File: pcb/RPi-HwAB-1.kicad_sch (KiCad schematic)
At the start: 5 parts, among them U1 CAT24C256

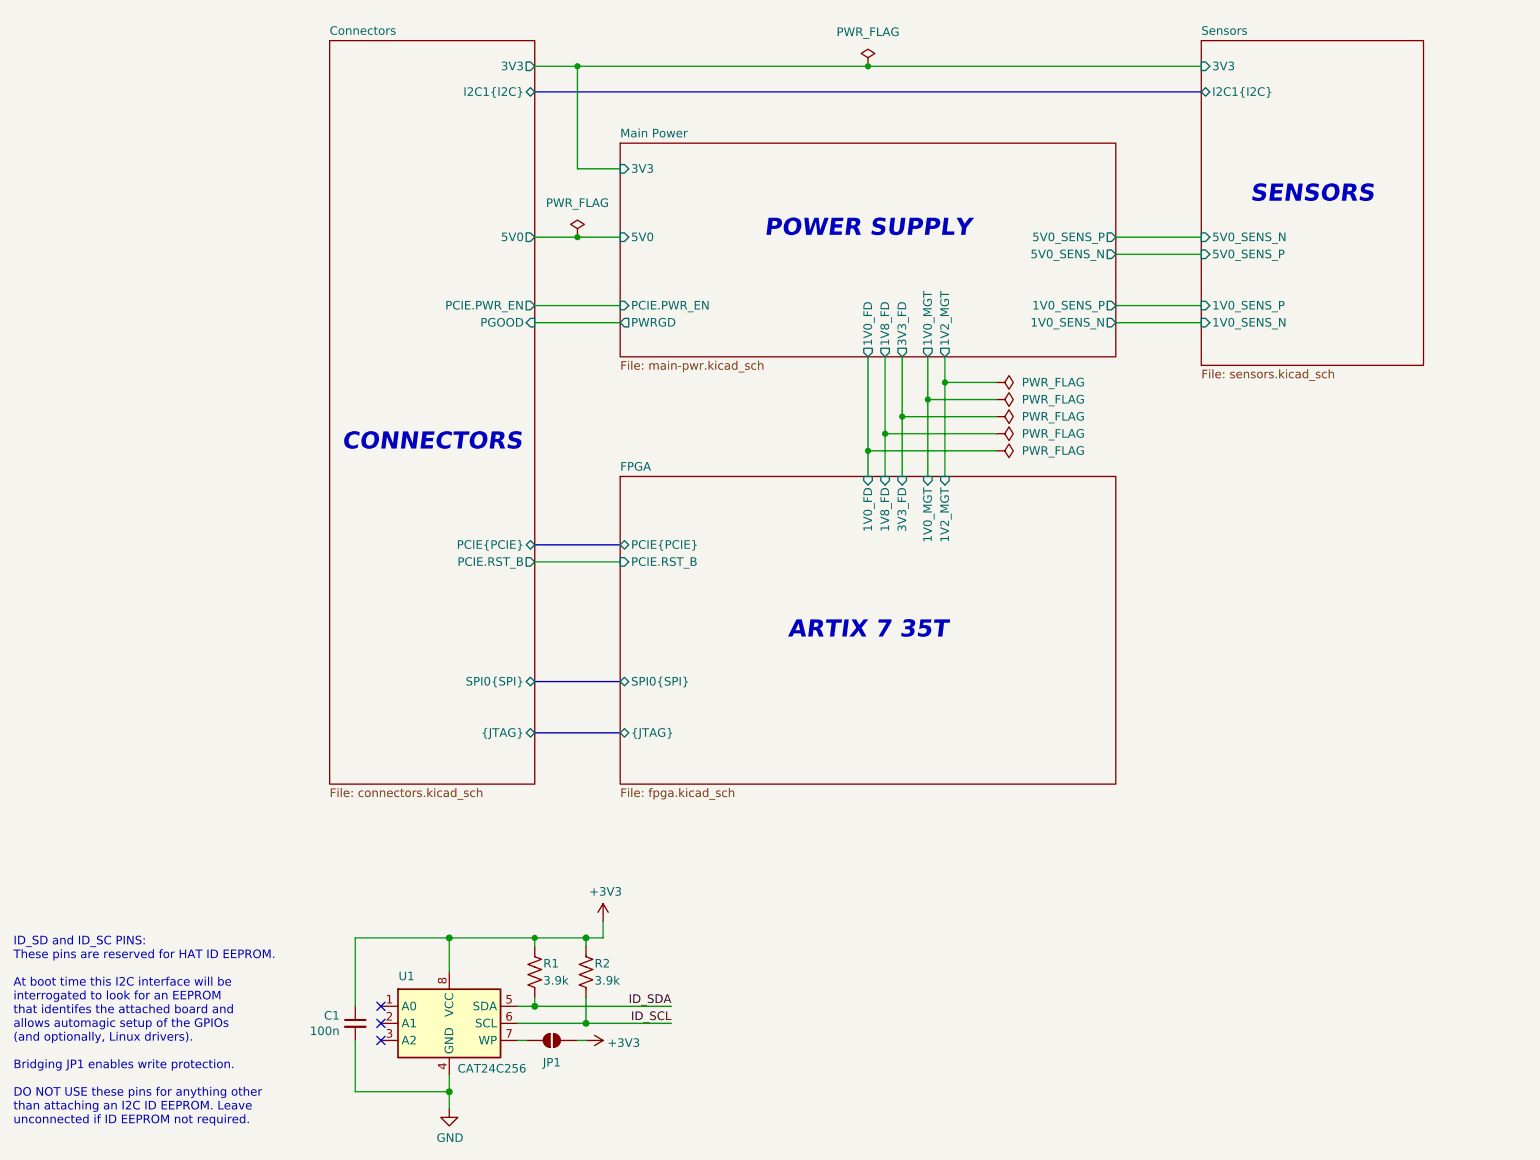
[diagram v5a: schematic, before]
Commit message: defined memory pinouts
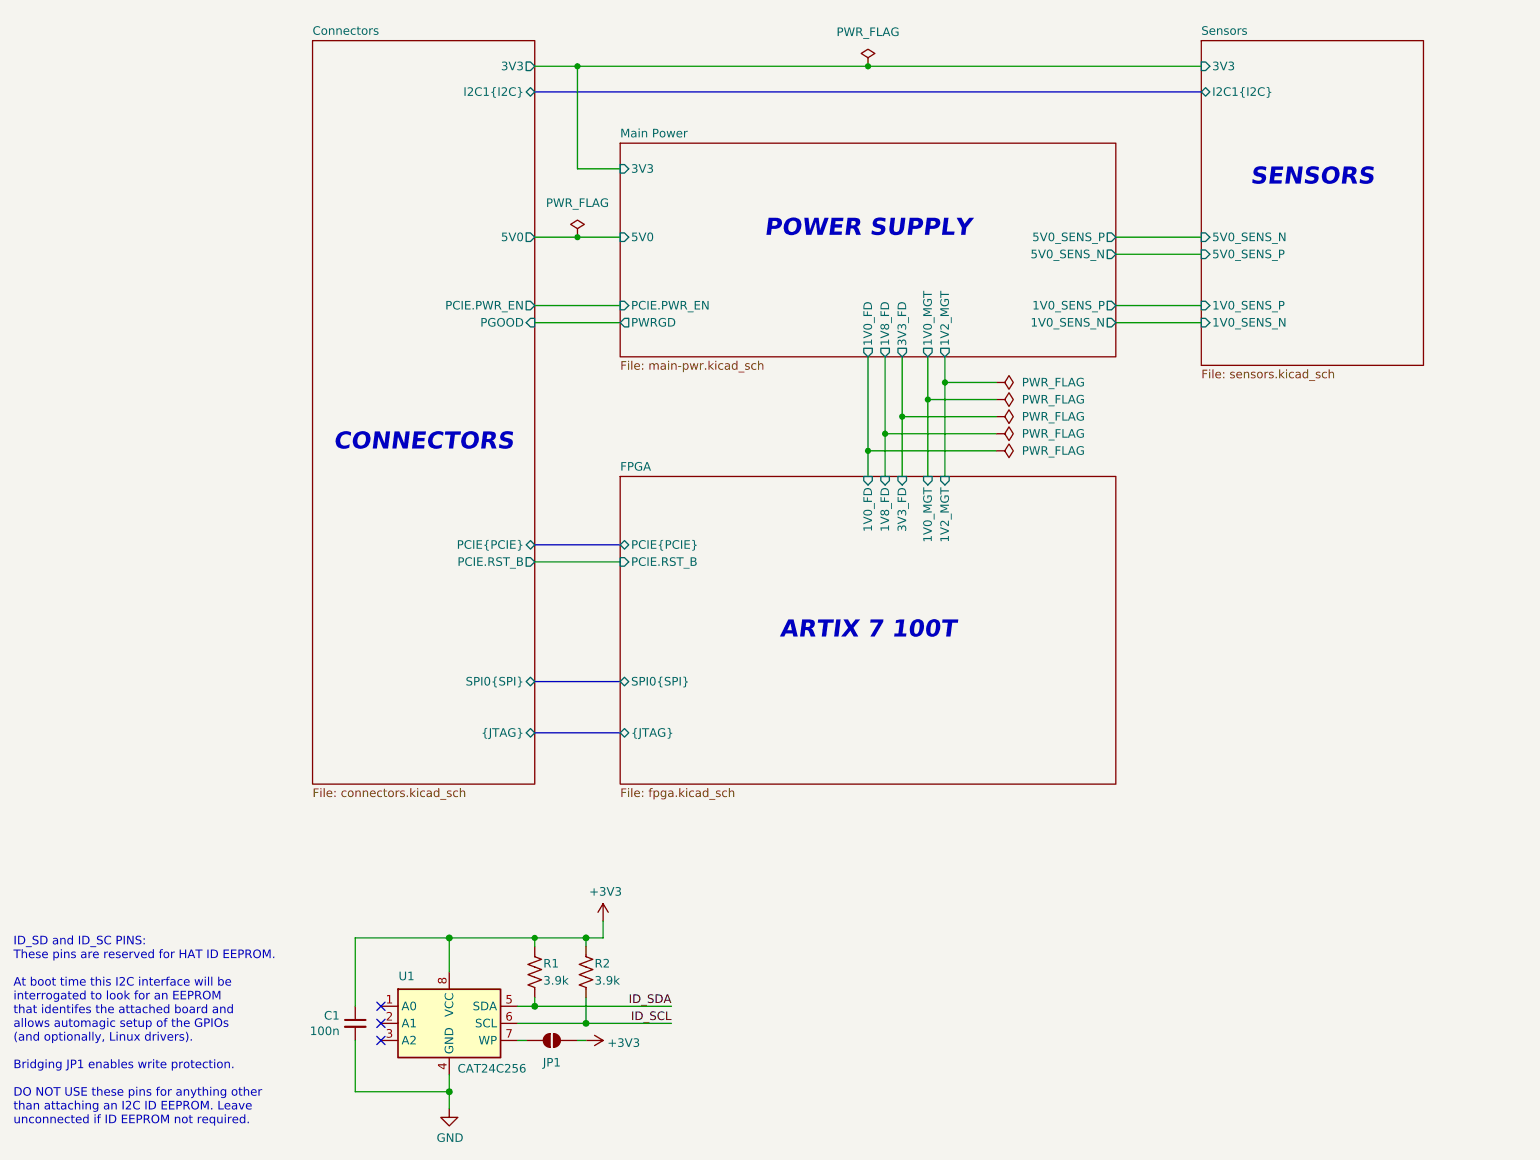
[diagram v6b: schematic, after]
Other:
- note added: "ARTIX 7 100T"
- note removed: "ARTIX 7 35T"
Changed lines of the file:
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@@
 		(members "MOSI" "MISO" "SCK" "CS0" "CS1")
 	)
-	(text "ARTIX 7 35T"
+	(text "ARTIX 7 100T"
 		(exclude_from_sim no)
 		(at 143.51 119.38 0)
@@
 	(text "SENSORS"
 		(exclude_from_sim no)
-		(at 209.55 54.61 0)
+		(at 209.55 52.07 0)
 		(effects
 			(font
@@
 	(text "CONNECTORS"
 		(exclude_from_sim no)
-		(at 78.74 91.44 0)
+		(at 77.47 91.44 0)
 		(effects
 			(font
@@
 		(at 143.51 35.56)
 		(diameter 0)
-		(color 0 0 0 0)
+		(color 0 0 255 1)
 	)
 	(junction
@@
 		(at 100.33 60.96)
 		(diameter 0)
-		(color 0 0 0 0)
+		(color 255 0 0 1)
 	)
 	(no_connect
@@
 		(on_board yes)
 		(dnp no)
-		(property "Reference" "#PWR07"
+		(property "Reference" "#PWR03"
 			(at 104.14 166.37 0)
 			(effects
@@
 			(project "RaspberryPi-HAT"
 				(path "/e63e39d7-6ac0-4ffd-8aa3-1841a4541b55"
-					(reference "#PWR07")
+					(reference "#PWR03")
 					(unit 1)
 				)
@@
 		(dnp no)
 		(fields_autoplaced yes)
-		(property "Reference" "#FLG07"
+		(property "Reference" "#FLG05"
 			(at 164.465 87.63 0)
 			(effects
@@
 			(project "RPi-HwAB-1"
 				(path "/e63e39d7-6ac0-4ffd-8aa3-1841a4541b55"
-					(reference "#FLG07")
+					(reference "#FLG05")
 					(unit 1)
 				)
@@
 		(dnp no)
 		(fields_autoplaced yes)
-		(property "Reference" "#FLG08"
+		(property "Reference" "#FLG04"
 			(at 164.465 85.09 0)
 			(effects
@@
 			(project "RPi-HwAB-1"
 				(path "/e63e39d7-6ac0-4ffd-8aa3-1841a4541b55"
-					(reference "#FLG08")
+					(reference "#FLG04")
 					(unit 1)
 				)
@@
 		(dnp no)
 		(fields_autoplaced yes)
-		(property "Reference" "#FLG011"
+		(property "Reference" "#FLG02"
 			(at 143.51 33.655 0)
 			(effects
@@
 			(project "RPi-HwAB-1"
 				(path "/e63e39d7-6ac0-4ffd-8aa3-1841a4541b55"
-					(reference "#FLG011")
+					(reference "#FLG02")
 					(unit 1)
 				)
@@
 		(on_board yes)
 		(dnp no)
-		(property "Reference" "#PWR05"
+		(property "Reference" "#PWR01"
 			(at 81.28 196.85 0)
 			(effects
@@
 			(project "RaspberryPi-HAT"
 				(path "/e63e39d7-6ac0-4ffd-8aa3-1841a4541b55"
-					(reference "#PWR05")
+					(reference "#PWR01")
 					(unit 1)
 				)
@@
 		(on_board yes)
 		(dnp no)
-		(property "Reference" "#PWR06"
+		(property "Reference" "#PWR02"
 			(at 97.79 180.34 0)
 			(effects
@@
 			(project "RaspberryPi-HAT"
 				(path "/e63e39d7-6ac0-4ffd-8aa3-1841a4541b55"
-					(reference "#PWR06")
+					(reference "#PWR02")
 					(unit 1)
 				)
@@
 		(dnp no)
 		(fields_autoplaced yes)
-		(property "Reference" "#FLG09"
+		(property "Reference" "#FLG03"
 			(at 164.465 82.55 0)
 			(effects
@@
 			(project "RPi-HwAB-1"
 				(path "/e63e39d7-6ac0-4ffd-8aa3-1841a4541b55"
-					(reference "#FLG09")
+					(reference "#FLG03")
 					(unit 1)
 				)
@@
 		(dnp no)
 		(fields_autoplaced yes)
-		(property "Reference" "#FLG05"
+		(property "Reference" "#FLG07"
 			(at 164.465 92.71 0)
 			(effects
@@
 			(project ""
 				(path "/e63e39d7-6ac0-4ffd-8aa3-1841a4541b55"
-					(reference "#FLG05")
+					(reference "#FLG07")
 					(unit 1)
 				)
@@
 		(dnp no)
 		(fields_autoplaced yes)
-		(property "Reference" "#FLG010"
+		(property "Reference" "#FLG01"
 			(at 100.33 59.055 0)
 			(effects
@@
 			(project "RPi-HwAB-1"
 				(path "/e63e39d7-6ac0-4ffd-8aa3-1841a4541b55"
-					(reference "#FLG010")
+					(reference "#FLG01")
 					(unit 1)
 				)
@@
 			(project "RPi-HwAB-1"
 				(path "/e63e39d7-6ac0-4ffd-8aa3-1841a4541b55"
-					(page "9")
+					(page "12")
 				)
 			)
@@
 			(project "RPi-HwAB-1"
 				(path "/e63e39d7-6ac0-4ffd-8aa3-1841a4541b55"
-					(page "3")
+					(page "5")
 				)
 			)
@@
 	)
 	(sheet
-		(at 63.5 31.75)
-		(size 30.48 110.49)
+		(at 60.96 31.75)
+		(size 33.02 110.49)
 		(exclude_from_sim no)
 		(in_bom yes)
@@
 		)
 		(property "Sheetname" "Connectors"
-			(at 63.5 31.0384 0)
+			(at 60.96 31.0384 0)
 			(effects
 				(font
@@
 		)
 		(property "Sheetfile" "connectors.kicad_sch"
-			(at 63.5 142.8246 0)
+			(at 60.96 142.8246 0)
 			(effects
 				(font
@@
 			(project "RPi-HwAB-1"
 				(path "/e63e39d7-6ac0-4ffd-8aa3-1841a4541b55"
-					(page "10")
-				)
-			)
+					(page "13")
+				)
+			)

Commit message: power restructuring
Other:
- sheet Main Power ports: added none; removed 1V0_FD, 1V0_MGT, 1V2_MGT, 1V8_FD, 3V3_FD

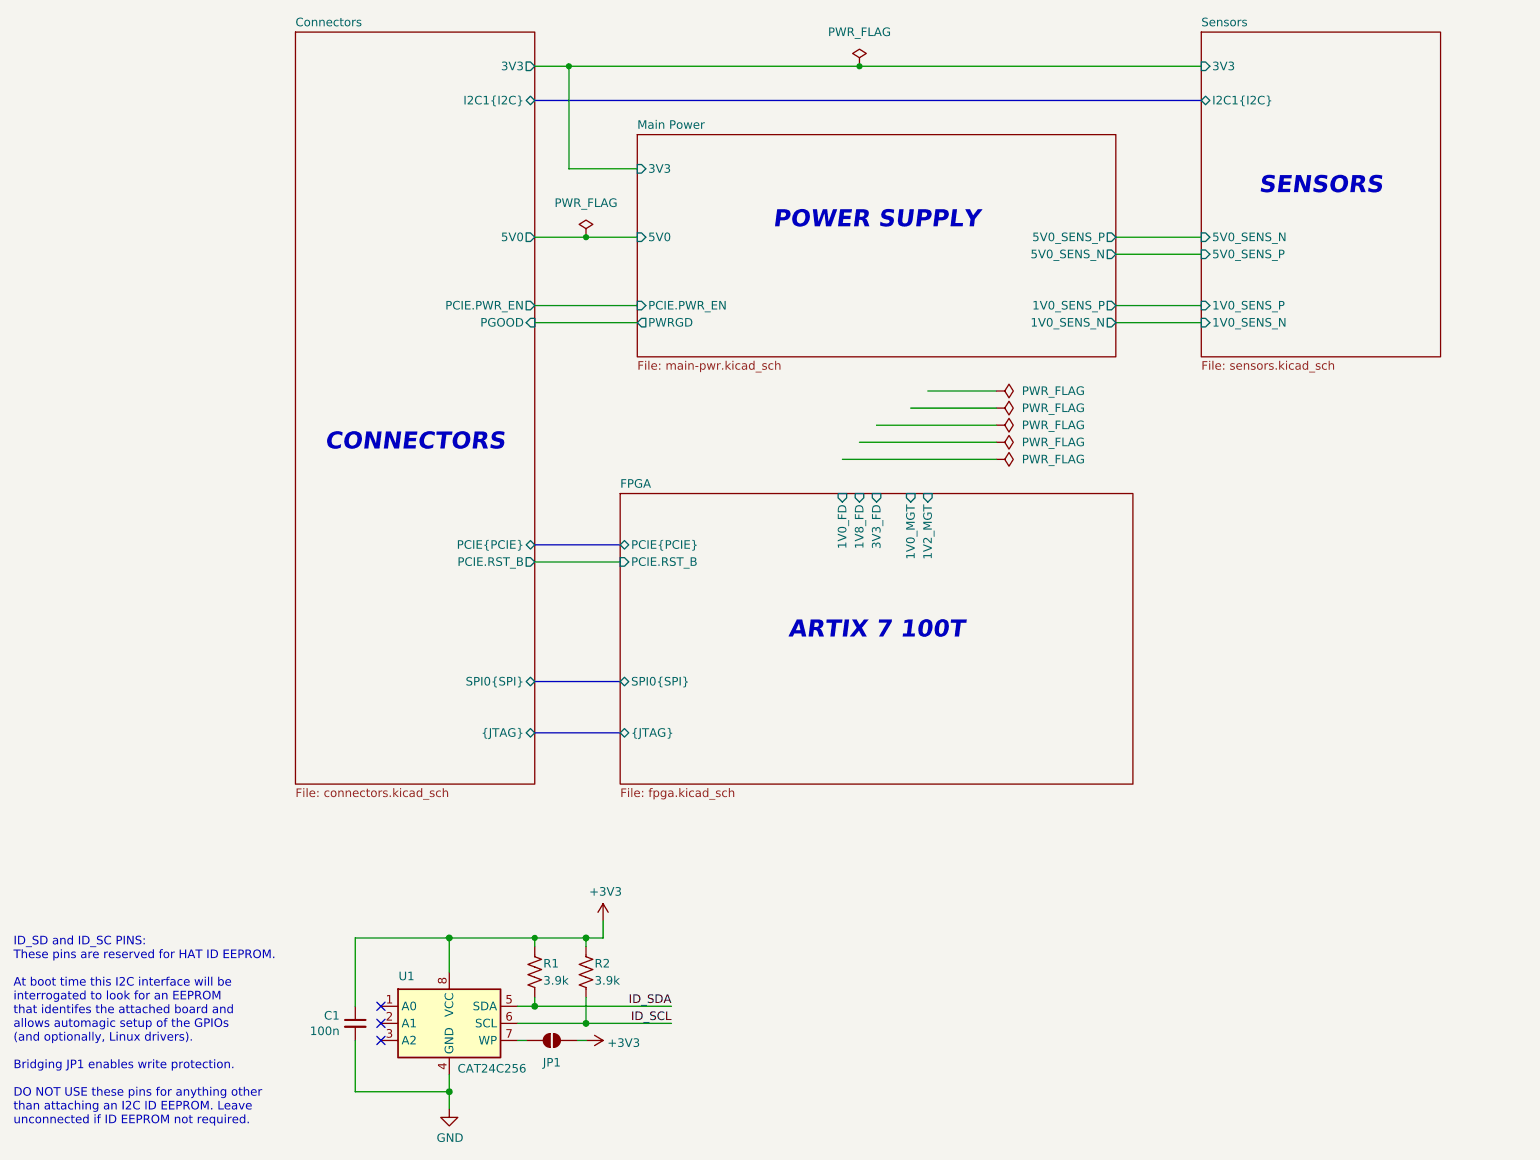
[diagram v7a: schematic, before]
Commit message: changes to power tree
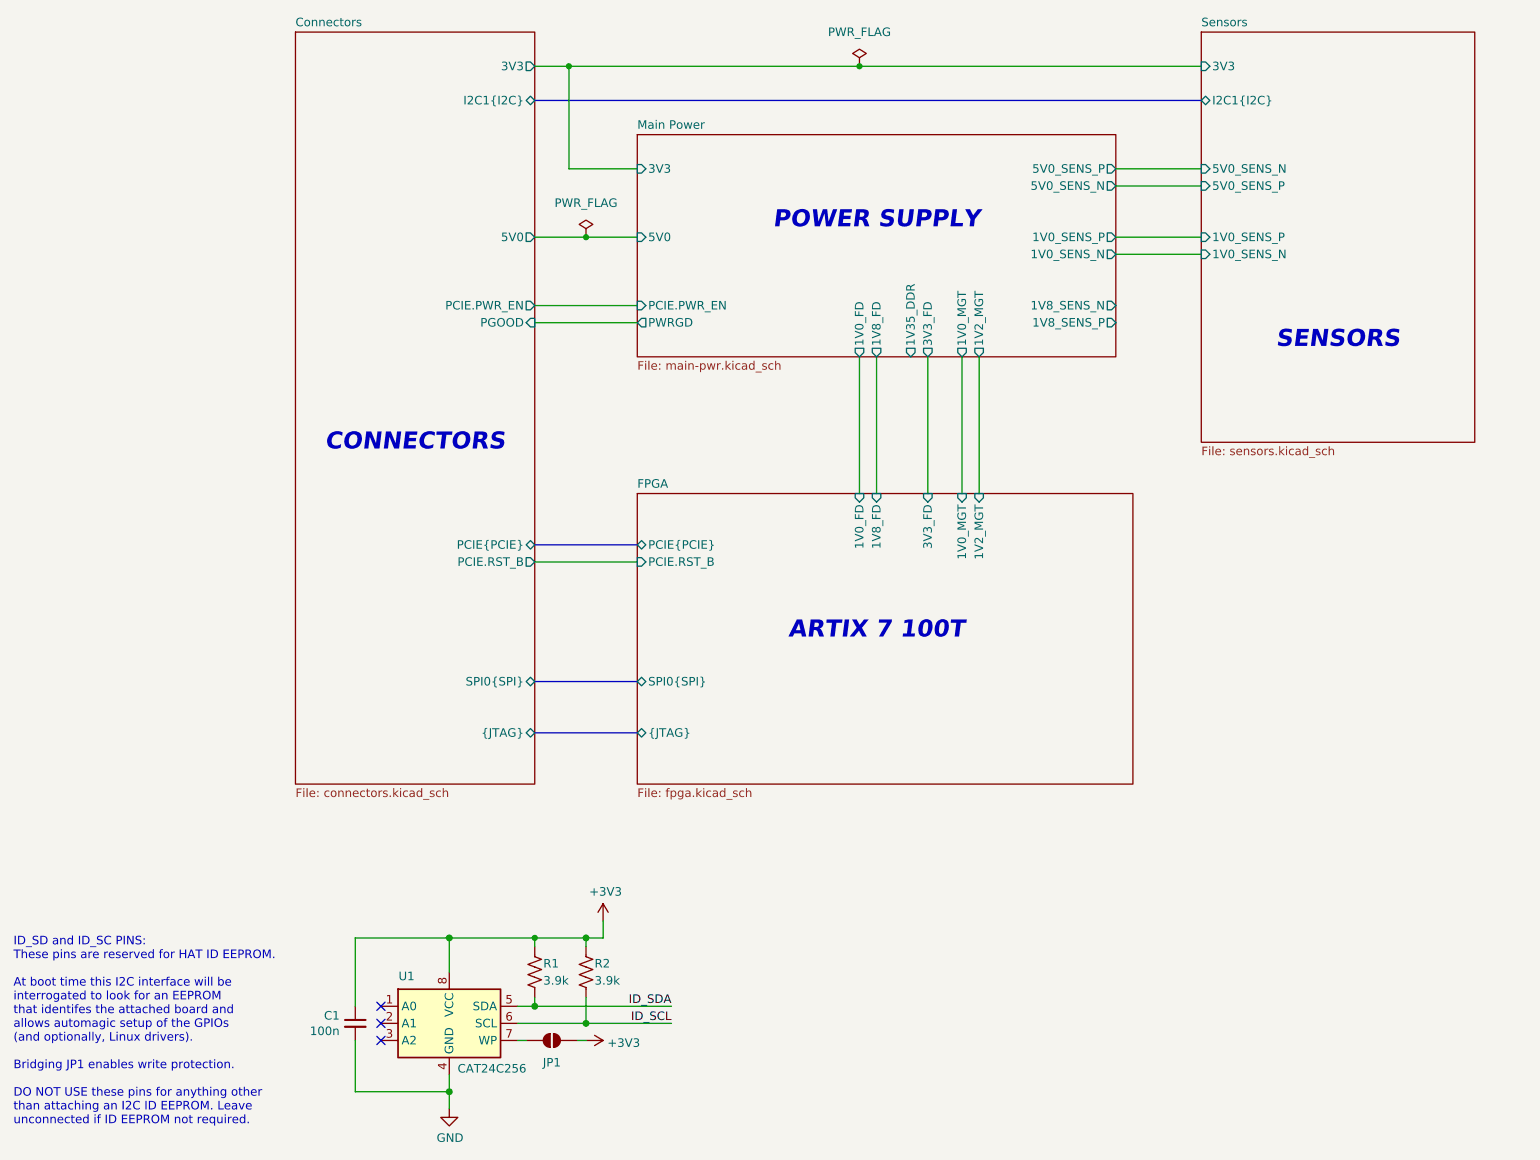
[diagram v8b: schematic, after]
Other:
- sheet Main Power ports: added 1V0_FD, 1V0_MGT, 1V2_MGT, 1V35_DDR, 1V8_FD, 1V8_SENS_N, 1V8_SENS_P, 3V3_FD; removed none
